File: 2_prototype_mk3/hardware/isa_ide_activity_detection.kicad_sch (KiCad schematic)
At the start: 16 parts, among them J3 Bus_ISA_8bit, J4 Conn_01x03, J5 Conn_01x03, U6 74LS573, U7 74LS573, U8 ATF22V10C-10PU

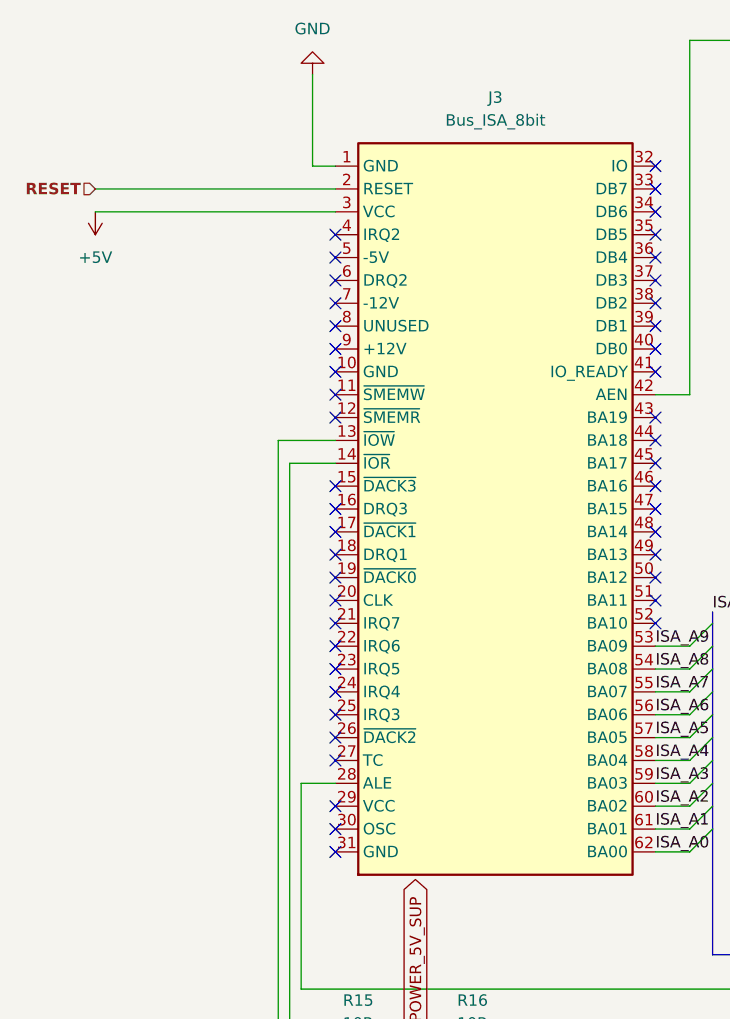
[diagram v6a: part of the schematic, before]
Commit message: Improve ground connections
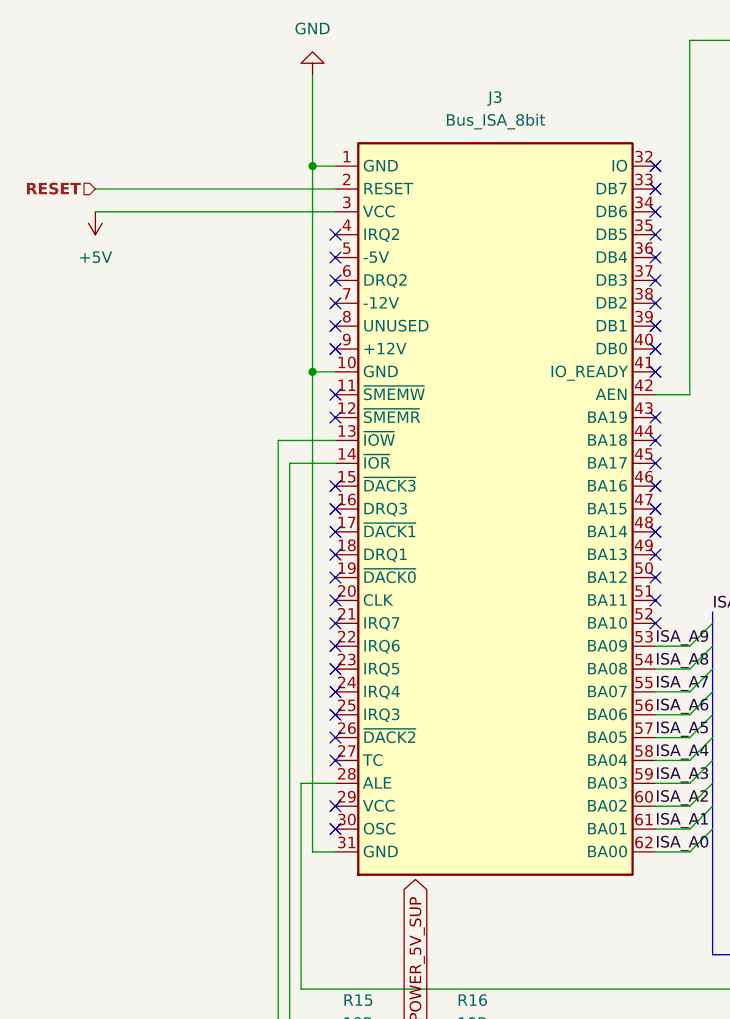
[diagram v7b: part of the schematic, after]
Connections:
- net GND: now also J3.10 (GND), J3.31 (GND)
- no-connect marks 63 -> 61
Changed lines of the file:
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@@
 	)
 	(junction
+		(at 81.28 55.88)
+		(diameter 0)
+		(color 0 0 0 0)
+	)
+	(junction
 		(at 152.4 77.47)
 		(diameter 0)
@@
 	)
 	(junction
+		(at 81.28 33.02)
+		(diameter 0)
+		(color 0 0 0 0)
+	)
+	(junction
 		(at 152.4 128.27)
 		(diameter 0)
@@
 	)
 	(no_connect
-		(at 83.82 55.88)
-	)
-	(no_connect
 		(at 222.25 73.66)
 	)
@@
 	)
 	(no_connect
-		(at 83.82 109.22)
-	)
-	(no_connect
 		(at 83.82 45.72)
 	)
@@
 		)
 	)
+	(wire
+		(pts
+			(xy 81.28 55.88) (xy 83.82 55.88)
+		)
+		(stroke
+			(width 0)
+			(type default)
+		)
+	)
 	(bus
 		(pts
@@
 	(wire
 		(pts
+			(xy 81.28 55.88) (xy 81.28 109.22)
+		)
+		(stroke
+			(width 0)
+			(type default)
+		)
+	)
+	(wire
+		(pts
 			(xy 143.51 45.72) (xy 146.05 45.72)
 		)
@@
 	(wire
 		(pts
+			(xy 81.28 109.22) (xy 83.82 109.22)
+		)
+		(stroke
+			(width 0)
+			(type default)
+		)
+	)
+	(wire
+		(pts
 			(xy 82.55 137.16) (xy 190.5 137.16)
 		)
@@
 	(wire
 		(pts
+			(xy 81.28 33.02) (xy 81.28 55.88)
+		)
+		(stroke
+			(width 0)
+			(type default)
+		)
+	)
+	(wire
+		(pts
 			(xy 195.58 78.74) (xy 196.85 78.74)
 		)
@@
 			)
 		)
-		(property "Datasheet" "74xx/74hc573.pdf"
+		(property "Datasheet" ""
 			(at 158.75 107.95 0)
 			(effects
@@
 			)
 		)
-		(property "Datasheet" "74xx/74hc573.pdf"
+		(property "Datasheet" ""
 			(at 158.75 55.88 0)
 			(effects

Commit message: Add LCSC component part numbers to BOM
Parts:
- D5: Manufacturer (none) -> onsemi / Taiwan Semi
- U6, U7: Manufacturer (none) -> Texas Instruments
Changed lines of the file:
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@@
+			)
+		)
+		(property "Manufacturer" ""
+			(at 222.25 53.34 90)
+			(effects
+				(font
+					(size 1.27 1.27)
+				)
+				(hide yes)
 			)
 		)
@@
 		)
 		(property "Manufacturer_Part_Number" "RC0603FR-0710RL"
+			(at 86.36 132.08 90)
+			(effects
+				(font
+					(size 1.27 1.27)
+				)
+				(hide yes)
+			)
+		)
+		(property "Manufacturer" ""
 			(at 86.36 132.08 90)
 			(effects
@@
 			)
 		)
+		(property "Manufacturer" ""
+			(at 209.55 76.2 0)
+			(effects
+				(font
+					(size 1.27 1.27)
+				)
+				(hide yes)
+			)
+		)
 		(pin "13"
 		)
@@
 			)
 		)
+		(property "Manufacturer" ""
+			(at 168.91 86.36 90)
+			(effects
+				(font
+					(size 1.27 1.27)
+				)
+				(hide yes)
+			)
+		)
 		(pin "1"
 		)
@@
 			)
 		)
+		(property "Manufacturer" "onsemi / Taiwan Semi"
+			(at 222.25 129.54 90)
+			(effects
+				(font
+					(size 1.27 1.27)
+				)
+				(hide yes)
+			)
+		)
 		(pin "2"
 		)
@@
 			)
 		)
+		(property "Manufacturer" "Texas Instruments"
+			(at 158.75 107.95 0)
+			(effects
+				(font
+					(size 1.27 1.27)
+				)
+				(hide yes)
+			)
+		)
 		(pin "11"
 		)
@@
 			)
 		)
+		(property "Manufacturer" ""
+			(at 101.6 71.12 0)
+			(effects
+				(font
+					(size 1.27 1.27)
+				)
+				(hide yes)
+			)
+		)
 		(pin "1"
 		)
@@
 			)
 		)
+		(property "Manufacturer" ""
+			(at 212.09 157.48 90)
+			(effects
+				(font
+					(size 1.27 1.27)
+				)
+				(hide yes)
+			)
+		)
 		(pin "2"
 		)
@@
 			)
 		)
+		(property "Manufacturer" ""
+			(at 99.06 132.08 90)
+			(effects
+				(font
+					(size 1.27 1.27)
+				)
+				(hide yes)
+			)
+		)
 		(pin "2"
 		)
@@
 			)
 		)
+		(property "Manufacturer" ""
+			(at 222.25 116.84 0)
+			(effects
+				(font
+					(size 1.27 1.27)
+				)
+				(hide yes)
+			)
+		)
 		(pin "2"
 		)
@@
 			)
 		)
+		(property "Manufacturer" ""
+			(at 167.64 33.02 90)
+			(effects
+				(font
+					(size 1.27 1.27)
+				)
+				(hide yes)
+			)
+		)
 		(pin "1"
 		)
@@
 			)
 		)
+		(property "Manufacturer" ""
+			(at 255.27 69.85 0)
+			(effects
+				(font
+					(size 1.27 1.27)
+				)
+				(hide yes)
+			)
+		)
 		(pin "3"
 		)
@@
 			)
 		)
+		(property "Manufacturer" "Texas Instruments"
+			(at 158.75 55.88 0)
+			(effects
+				(font
+					(size 1.27 1.27)
+				)
+				(hide yes)
+			)
+		)
 		(pin "11"
 		)
@@
 			)
 		)
+		(property "Manufacturer" ""
+			(at 255.27 81.28 0)
+			(effects
+				(font
+					(size 1.27 1.27)
+				)
+				(hide yes)
+			)
+		)
 		(pin "3"
 		)
@@
 			)
 		)
+		(property "Manufacturer" ""
+			(at 212.09 146.05 90)
+			(effects
+				(font
+					(size 1.27 1.27)
+				)
+				(hide yes)
+			)
+		)
 		(pin "2"
 		)
@@
 			(at 212.09 135.89 90)
 			(effects
+				(font
+					(size 1.27 1.27)
+				)
+				(hide yes)
+			)
+		)
+		(property "Manufacturer" ""
+			(at 212.09 135.89 90)
+			(effects
